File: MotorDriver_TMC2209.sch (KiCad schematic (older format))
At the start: 16 parts

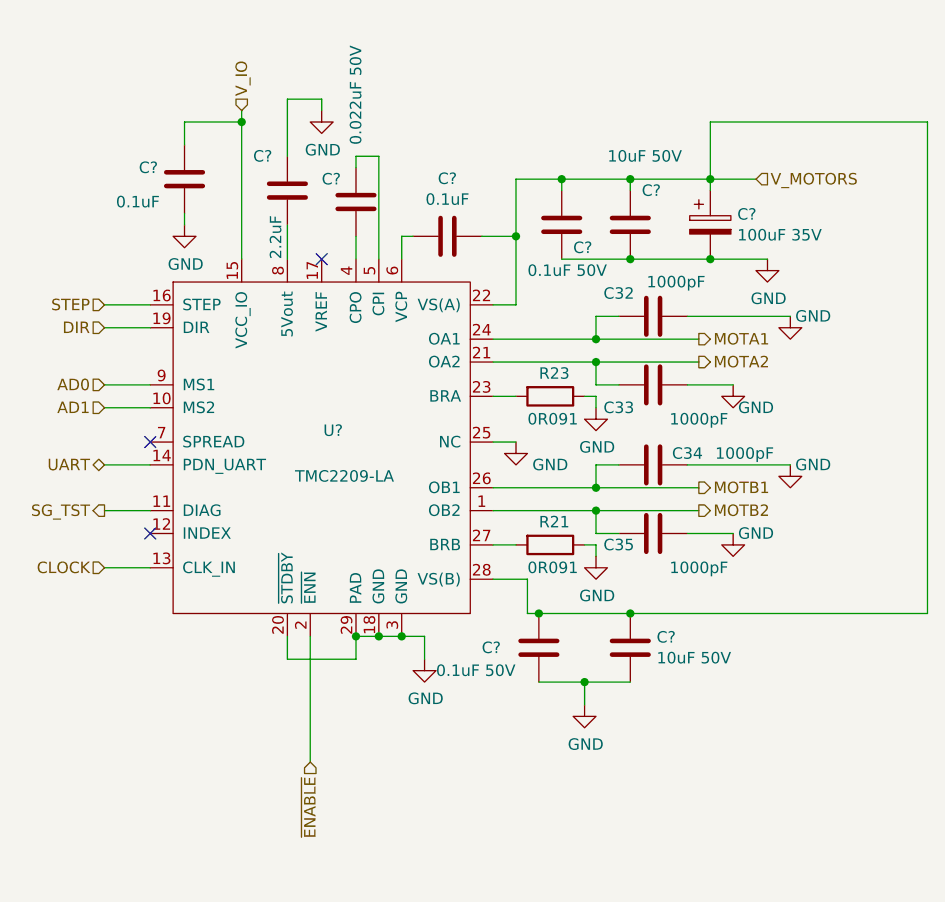
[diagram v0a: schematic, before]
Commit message: Finished the schematics wiring and reset the routing.
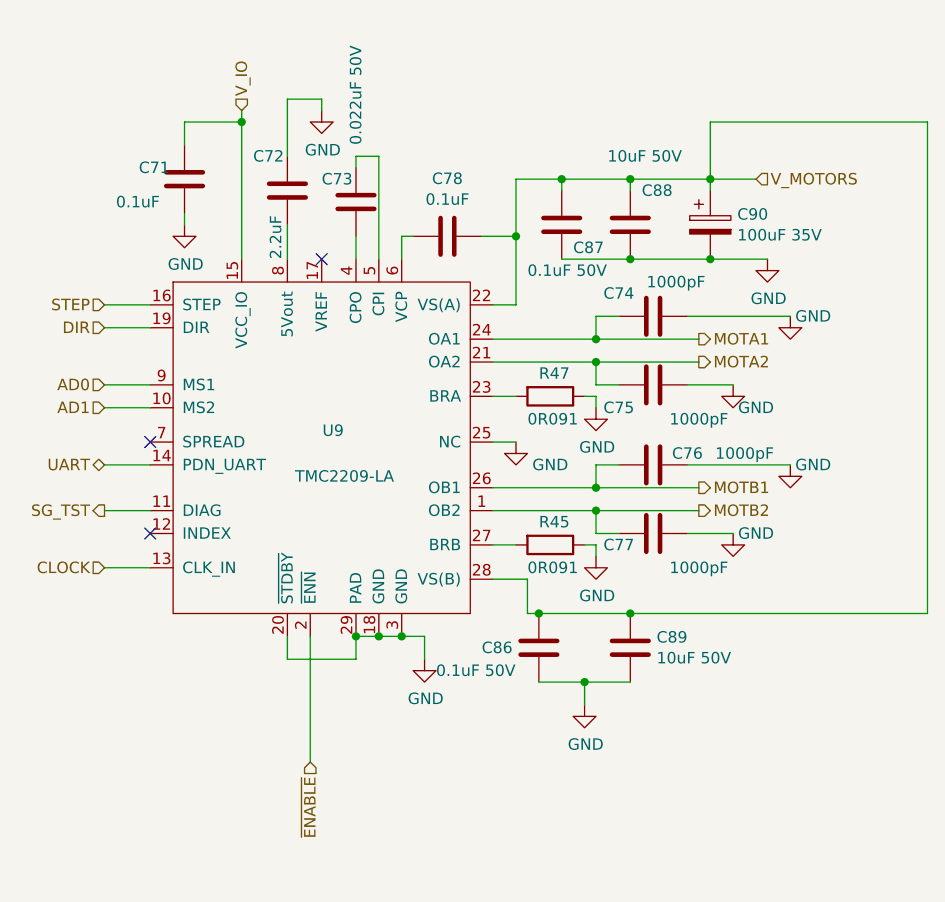
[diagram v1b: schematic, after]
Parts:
- C26, C27, C28, C29: renamed from C?; footprint (none) -> PrntrBoardV1:C_0603_1608Metric
- C30, C31: renamed from C?; footprint (none) -> PrntrBoardV1:C_0402_1005Metric
- C36, C39: renamed from C?; footprint (none) -> PrntrBoardV1:C_1206_3216Metric
- C40: renamed from C?; footprint (none) -> Capacitor_SMD:CP_Elec_6.3x7.7
- U6: renamed from U?; footprint (none) -> PrntrBoardV1:TMC22xx_QFN
